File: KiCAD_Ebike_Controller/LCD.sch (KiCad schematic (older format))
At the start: 16 parts, among them J10 I2C_SCL, J11 I2C_SDA, Q7 BCV62, Q8 BCV62, Q9 2N7000, U3 PCF8574

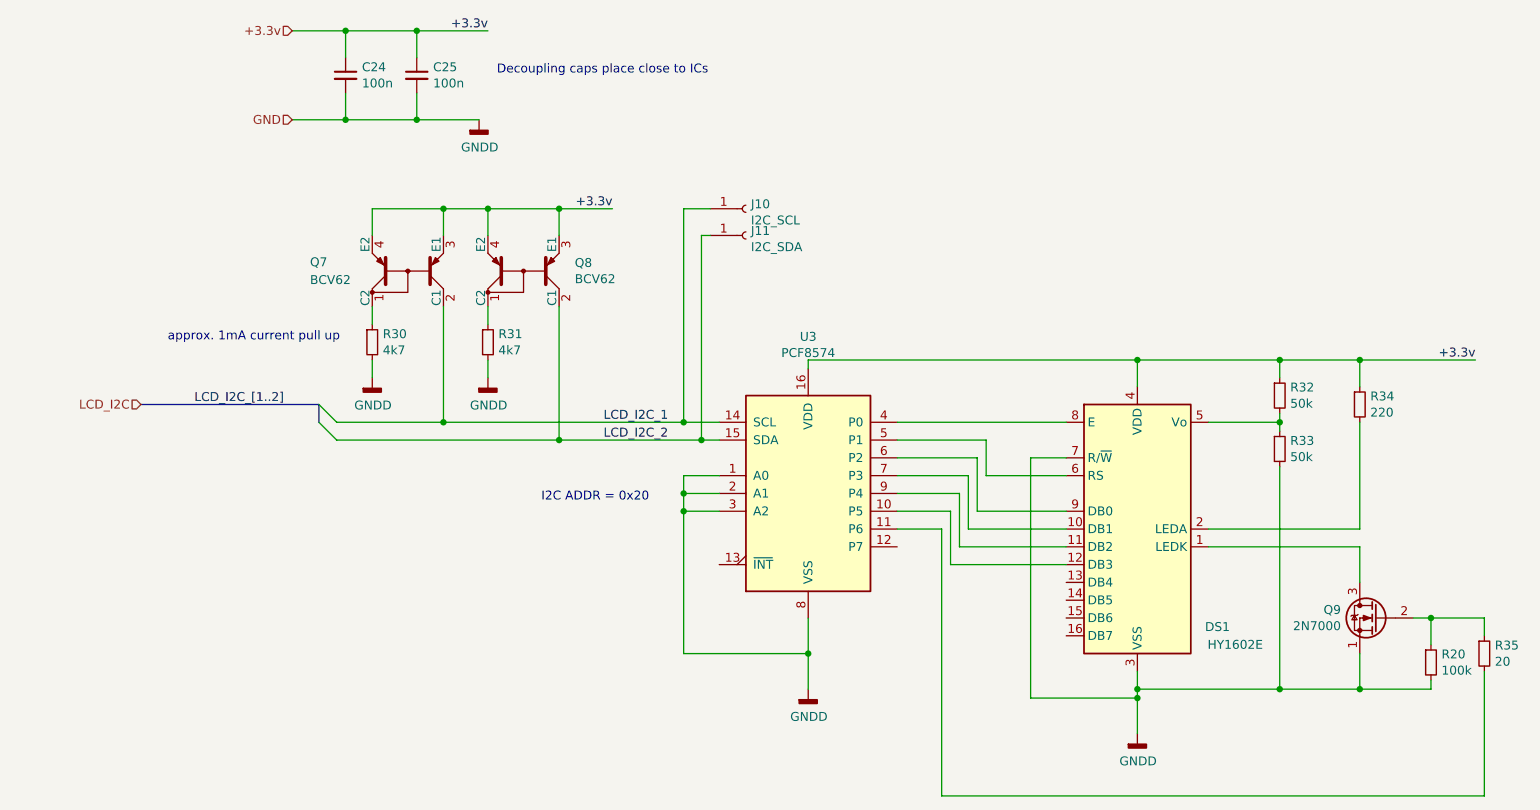
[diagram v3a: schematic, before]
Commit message: Layout done. will tidy up ref des next
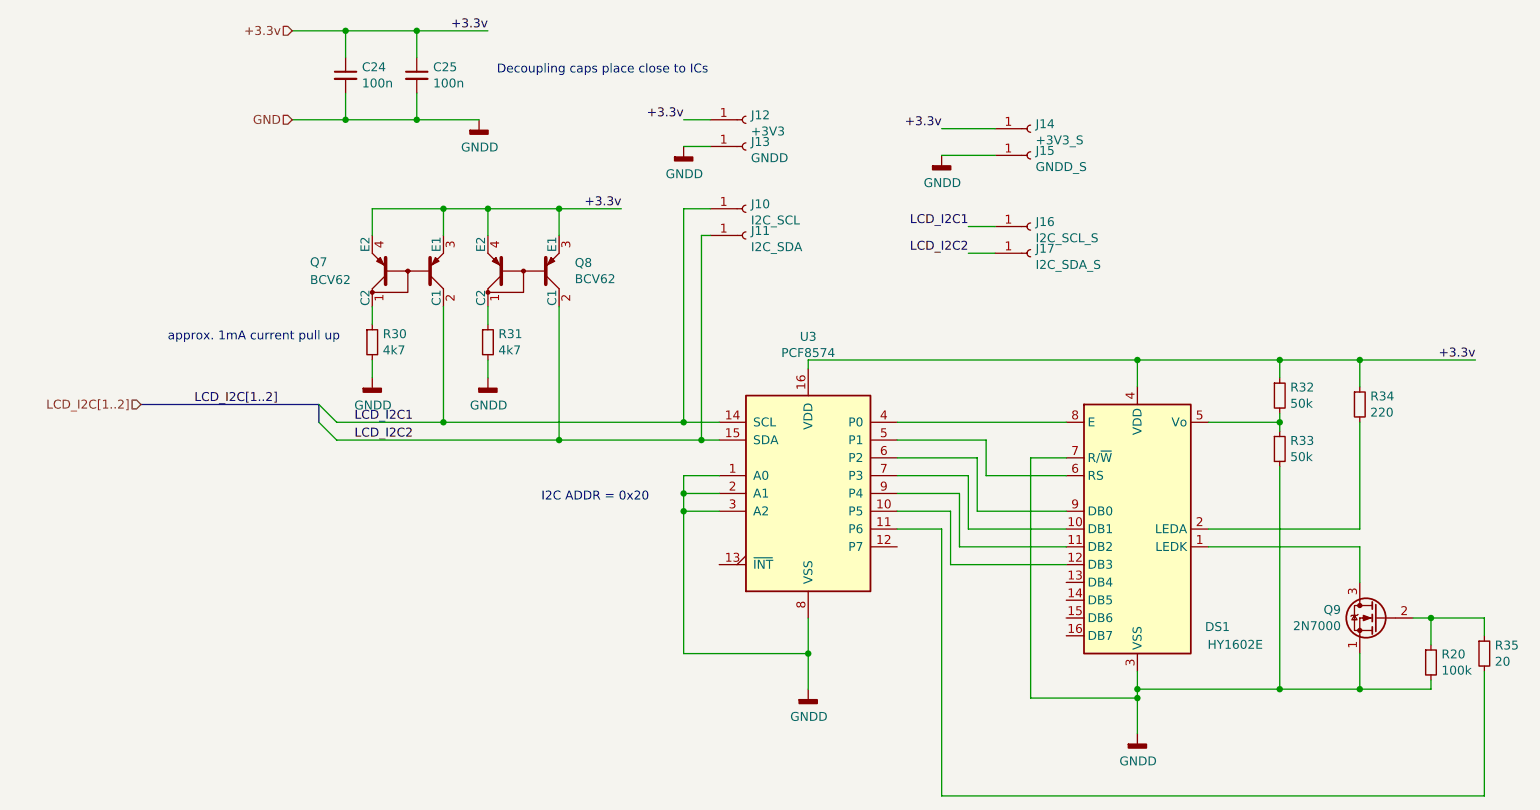
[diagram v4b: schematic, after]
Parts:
- added J12: +3V3, Connector_PinHeader_2.54mm:PinHeader_1x01_P2.54mm_Vertical, symbol Connector:Conn_01x01_Female
- added J13: GNDD, Connector_PinHeader_2.54mm:PinHeader_1x01_P2.54mm_Vertical, symbol Connector:Conn_01x01_Female
- added J14: +3V3_S, Connector_PinHeader_2.54mm:PinHeader_1x01_P2.54mm_Vertical, symbol Connector:Conn_01x01_Female
- added J15: GNDD_S, Connector_PinHeader_2.54mm:PinHeader_1x01_P2.54mm_Vertical, symbol Connector:Conn_01x01_Female
- added J16: I2C_SCL_S, Connector_PinHeader_2.54mm:PinHeader_1x01_P2.54mm_Vertical, symbol Connector:Conn_01x01_Female
- added J17: I2C_SDA_S, Connector_PinHeader_2.54mm:PinHeader_1x01_P2.54mm_Vertical, symbol Connector:Conn_01x01_Female
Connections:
- net +3.3v: now also J12.1 (Pin_1), J14.1 (Pin_1)
- net GNDD: now also J13.1 (Pin_1), J15.1 (Pin_1)
- net LCD_I2C_1 renamed LCD_I2C1
- net LCD_I2C1: now also J16.1 (Pin_1)
- net LCD_I2C_2 renamed LCD_I2C2
- net LCD_I2C2: now also J17.1 (Pin_1)
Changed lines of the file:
@@
 $Descr A4 11693 8268
 encoding utf-8
-Sheet 4 7
+Sheet 3 7
 Title ""
 Date ""
@@
 Connection ~ 4850 4650
 Entry Wire Line
-	2100 3350 2200 3450
-Entry Wire Line
 	2100 3250 2200 3350
-Wire Bus Line
-	2100 3350 2100 3250
-Wire Bus Line
-	2100 3250 1100 3250
 Wire Wire Line
 	2200 3350 2800 3350
@@
 Text Notes 3350 3800 0    50   ~ 0
 I2C ADDR = 0x20
-Text HLabel 1100 3250 0    50   Input ~ 0
-LCD_I2C
-Text Label 1400 3250 0    50   ~ 0
-LCD_I2C_[1..2]
-Text Label 3700 3350 0    50   ~ 0
-LCD_I2C_1
-Text Label 3700 3450 0    50   ~ 0
-LCD_I2C_2
+Text Label 2300 3350 0    50   ~ 0
+LCD_I2C1
 Text HLabel 1950 1150 0    50   Input ~ 0
 +3.3v
@@
 	2800 2150 3050 2150
 Wire Wire Line
-	3450 2150 3750 2150
+	3450 2150 3800 2150
 Connection ~ 3450 2150
-Text Label 3750 2150 2    50   ~ 0
+Text Label 3800 2150 2    50   ~ 0
 +3.3v
 $Comp
@@
 	1    0    0    -1
 $EndComp
+Entry Wire Line
+	2100 3350 2200 3450
+Wire Bus Line
+	2100 3350 2100 3250
+Text HLabel 1100 3250 0    50   Input ~ 0
+LCD_I2C[1..2]
+Wire Bus Line
+	2100 3250 1100 3250
+Text Label 1400 3250 0    50   ~ 0
+LCD_I2C[1..2]
+Text Label 2300 3450 0    50   ~ 0
+LCD_I2C2
+$Comp
+L Connector:Conn_01x01_Female J12
+U 1 1 6004AD63
+P 4500 1650
+F 0 "J12" H 4528 1676 50  0000 L CNN
+F 1 "+3V3" H 4528 1585 50  0000 L CNN
+F 2 "Connector_PinHeader_2.54mm:PinHeader_1x01_P2.54mm_Vertical" H 4500 1650 50  0001 C CNN
+F 3 "~" H 4500 1650 50  0001 C CNN
+	1    4500 1650
+	1    0    0    -1
+$EndComp
+$Comp
+L Connector:Conn_01x01_Female J13
+U 1 1 6004AD69
+P 4500 1800
+F 0 "J13" H 4528 1826 50  0000 L CNN
+F 1 "GNDD" H 4528 1735 50  0000 L CNN
+F 2 "Connector_PinHeader_2.54mm:PinHeader_1x01_P2.54mm_Vertical" H 4500 1800 50  0001 C CNN
+F 3 "~" H 4500 1800 50  0001 C CNN
+	1    4500 1800
+	1    0    0    -1
+$EndComp
+Wire Wire Line
+	4300 1650 4150 1650
+Text Label 4150 1650 2    50   ~ 0
++3.3v
+$Comp
+L power:GNDD #PWR0131
+U 1 1 600524F2
+P 4150 1800
+F 0 "#PWR0131" H 4150 1550 50  0001 C CNN
+F 1 "GNDD" H 4154 1645 50  0000 C CNN
+F 2 "" H 4150 1800 50  0001 C CNN
+F 3 "" H 4150 1800 50  0001 C CNN
+	1    4150 1800
+	1    0    0    -1
+$EndComp
+Wire Wire Line
+	4300 1800 4150 1800
+$Comp
+L Connector:Conn_01x01_Female J16
+U 1 1 6008752C
+P 6100 2250
+F 0 "J16" H 6128 2276 50  0000 L CNN
+F 1 "I2C_SCL_S" H 6128 2185 50  0000 L CNN
+F 2 "Connector_PinHeader_2.54mm:PinHeader_1x01_P2.54mm_Vertical" H 6100 2250 50  0001 C CNN
+F 3 "~" H 6100 2250 50  0001 C CNN
+	1    6100 2250
+	1    0    0    -1
+$EndComp
+$Comp
+L Connector:Conn_01x01_Female J17
+U 1 1 60087532
+P 6100 2400
+F 0 "J17" H 6128 2426 50  0000 L CNN
+F 1 "I2C_SDA_S" H 6128 2335 50  0000 L CNN
+F 2 "Connector_PinHeader_2.54mm:PinHeader_1x01_P2.54mm_Vertical" H 6100 2400 50  0001 C CNN
+F 3 "~" H 6100 2400 50  0001 C CNN
+	1    6100 2400
+	1    0    0    -1
+$EndComp
+Wire Wire Line
+	5900 2250 5750 2250
+$Comp
+L Connector:Conn_01x01_Female J14
+U 1 1 6008753A
+P 6100 1700
+F 0 "J14" H 6128 1726 50  0000 L CNN
+F 1 "+3V3_S" H 6128 1635 50  0000 L CNN
+F 2 "Connector_PinHeader_2.54mm:PinHeader_1x01_P2.54mm_Vertical" H 6100 1700 50  0001 C CNN
+F 3 "~" H 6100 1700 50  0001 C CNN
+	1    6100 1700
+	1    0    0    -1
+$EndComp
+$Comp
+L Connector:Conn_01x01_Female J15
+U 1 1 60087540
+P 6100 1850
+F 0 "J15" H 6128 1876 50  0000 L CNN
+F 1 "GNDD_S" H 6128 1785 50  0000 L CNN
+F 2 "Connector_PinHeader_2.54mm:PinHeader_1x01_P2.54mm_Vertical" H 6100 1850 50  0001 C CNN
+F 3 "~" H 6100 1850 50  0001 C CNN
+	1    6100 1850
+	1    0    0    -1
+$EndComp
+Text Label 5750 2400 2    50   ~ 0
+LCD_I2C2
+Text Label 5750 2250 2    50   ~ 0
+LCD_I2C1
+Wire Wire Line
+	5750 2400 5900 2400
+Text Label 5600 1700 2    50   ~ 0
++3.3v
+$Comp
+L power:GNDD #PWR0137
+U 1 1 600A6F4F
+P 5600 1850
+F 0 "#PWR0137" H 5600 1600 50  0001 C CNN
+F 1 "GNDD" H 5604 1695 50  0000 C CNN
+F 2 "" H 5600 1850 50  0001 C CNN
+F 3 "" H 5600 1850 50  0001 C CNN
+	1    5600 1850
+	1    0    0    -1
+$EndComp
+Wire Wire Line
+	5600 1700 5900 1700
+Wire Wire Line
+	5600 1850 5900 1850
 $EndSCHEMATC
